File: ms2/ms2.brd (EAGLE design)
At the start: 100 x 100 mm, 127 parts, among them J1 POWERPOLE_POWER25A, J10 RS485_1, J11 I2C, J12 TTL_SERIAL, J13 Radio, J14 RS485_3, J2 RAIN, J3 ADC1, J4 ON, J5 D1, J6 D2, J7 ADC2, J8 LED-EN, J9 RS485_2, Q1 DMG6602SVT, Q2 DMG6602SVT, Q3 DMG6602SVT, Q4 DMG6602SVT, U1 LT1934ES6TRMPBF, U2 LT1934ES6TRMPBF, U3 DS3231SN, U4 ISL3179EIBZ, U5 ISL3179EIBZ, U6 ISL3179EIBZ, X1 KUSBVX-BS1N

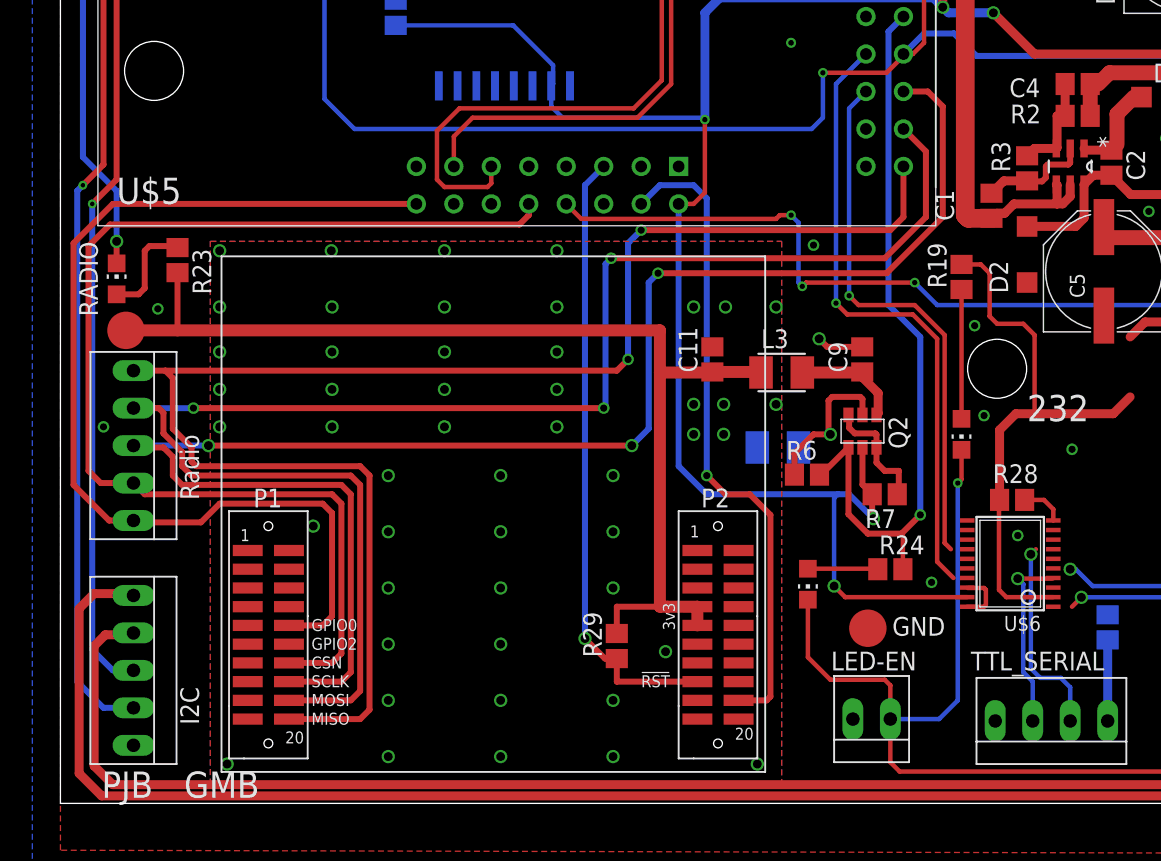
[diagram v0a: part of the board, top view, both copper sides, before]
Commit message: CC1120 rotated
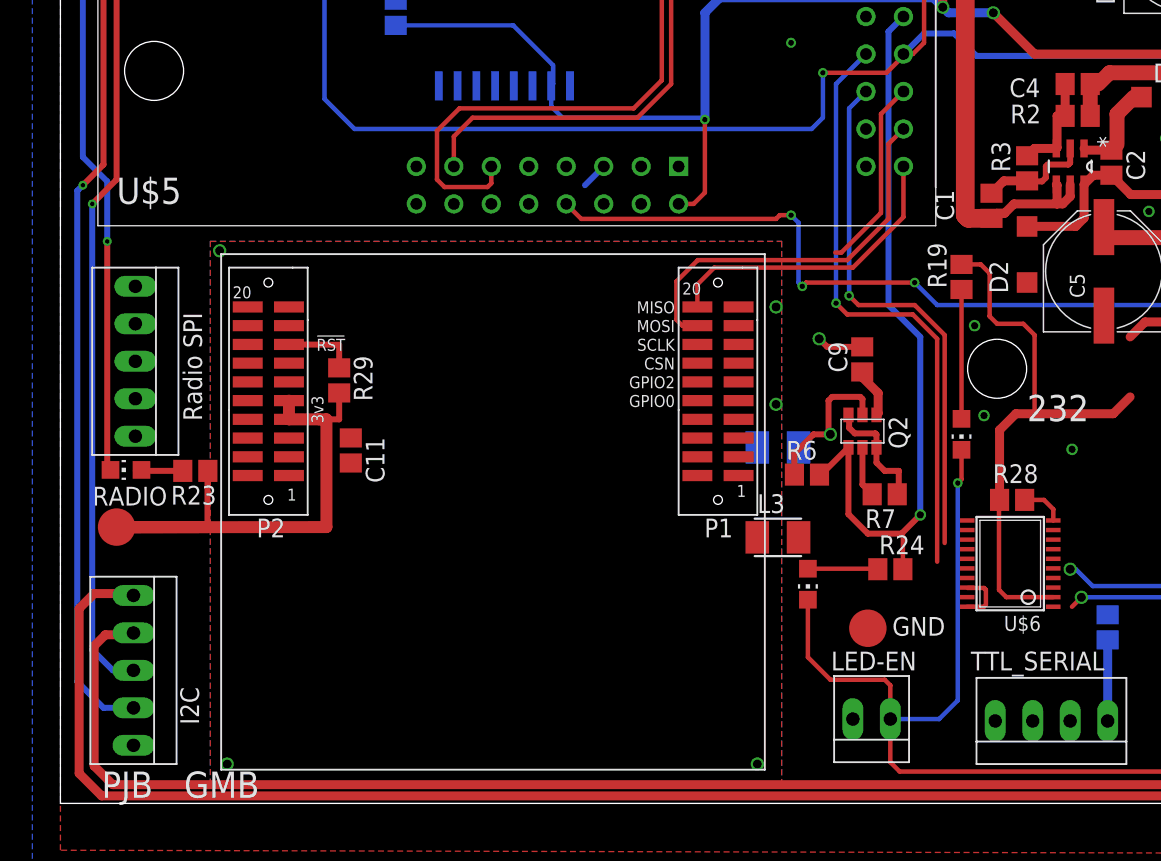
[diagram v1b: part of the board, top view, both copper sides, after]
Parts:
- J13: value Radio -> Radio SPI
- moved R29 26.0 mm to (18.9, 28.7), turned to 270 degrees
- moved C11 25.3 mm to (19.7, 23.9), turned to 270 degrees
- moved U$8 16.5 mm to (29.5, 27.9), turned to 180 degrees
- moved R23 14.3 mm to (9.14, 22.5), turned to 0 degrees
- moved RADIO_VCC 13.4 mm to (3.81, 18.7)
- moved LED8 13.0 mm to (4.45, 22.6), turned to 90 degrees
- moved L3 11.2 mm to (48.6, 18.0)
- moved J13 5.72 mm to (4.95, 28.8)
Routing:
- net SPI_CLK: track 111.0 -> 13.1 mm, vias 3 -> 0
- net SPI_SOMI: track 105.5 -> 20.8 mm, vias 2 -> 0
- net SPI_SIMO: track 109.3 -> 26.8 mm, vias 3 -> 0
- net RADIO_CSN: track 78.8 -> 0.00 mm
- net RADIO_INT: track 70.8 -> 0.00 mm
- net VCC_3V3: track 245.7 -> 195.8 mm, vias 8 -> 6
- net RADIO_CCA_STATUS: track 44.1 -> 0.00 mm, vias 1 -> 0
- net RADIO_!RST: track 42.3 -> 6.76 mm, vias 1 -> 0
- net RADIO_3V3: track 74.8 -> 44.2 mm
- net LGND: track 380.5 -> 394.4 mm
- net TTL_TX: track 13.7 -> 0.00 mm, vias 1 -> 0
- net TTL_RX: track 12.4 -> 0.00 mm, vias 1 -> 0
- net N$24: track 7.47 -> 3.41 mm
- net N$108: track 7.01 -> 3.57 mm
- net UART1_RX: track 45.9 -> 44.3 mm
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
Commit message: Work on MS2
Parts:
- moved J11 118.1 mm to (122.9, 11.2)
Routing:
- net SENSE_3V3: track 327.0 -> 178.7 mm
- net SENSE_5V: track 224.8 -> 99.6 mm
- net SCL: track 113.1 -> 0.00 mm, vias 2 -> 0
- net SDA: track 110.4 -> 0.00 mm, vias 2 -> 0
- net GND: track 29.6 -> 0.00 mm, vias 19 -> 0

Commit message: Added LTSpice schematic of Switch mode + LDO combo.
Work on MS2.
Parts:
- removed JP3: (no value), SparkFun-Passives:SJ_2S
- removed L2, L6: 20uH, rcl:6000-XXXX-RC
- added 12V_OUT: POWERPOLE_POWER25A, powerpoles:POWERPOLE_PAIR_25A
- added 3.4V: TPB2,54, testpad:B2,54
- added C23: 0.1uF, resistor:C0805
- added C24: 100uF, rcl:PANASONIC_E
- added D10, D6, D7, D8, D9: (no value), diode:SMB
- added D11, D12: MBR0530T1G, diode:SOD123
- added F10, F11, F12, F13, F14: MCF0805, farnell-parts:0805
- added JP4: PS EN, pinhead:1X02
- added JP6: 3.3V Out EN, pinhead:1X02
- added Q5: DMG6602SVT, farnell-parts:TSOT26
- added R33, R35: 100K, resistor:R0805
- added R34, R36, R37: 1M, resistor:R0805
- added U7: TPD2E001IDRLRQ1, Texas Instruments_By_element14_Batch_1:SOT50P160X60-5N
- added U8, U9: TPS79333DBVR, CC11x:SOT95P280X145-5N
- C16: value 330uF -> 1uF; device rcl:E5-8,5 -> resistor:C0805
- C17: value (none) -> 0.1uF
- C18: value (none) -> 2.2uF; device resistor:B/3528-21R -> resistor:C0805
- C6: value 330uF -> 2.2uF; device rcl:E5-8,5 -> resistor:C0805
- C7: value (none) -> 100uF; device resistor:C0805 -> rcl:PANASONIC_E
- C8: value (none) -> 1uF; device resistor:B/3528-21R -> resistor:C0805
- JP1: device SparkFun-Passives:SJ_2S-NO -> pinhead:1X05
- JP2: value (none) -> 5V Out EN; device SparkFun-Passives:SJ_2S-NO -> pinhead:1X02
- R3: value 604K -> 562K
- R4: value 100K -> 1M
- moved C18 405.4 mm to (0.00, -315.7), turned to 0 degrees
- moved C17 386.0 mm to (0.00, -310.1), turned to 0 degrees
- moved C16 378.4 mm to (0.00, -294.1)
- moved JP1 206.2 mm to (4.83, -143.1), turned to 0 degrees
- moved JP2 193.4 mm to (1.02, -95.9), turned to 0 degrees
- moved R12 171.4 mm to (-0.10, -120.0)
- moved R4 111.8 mm to (115.0, 47.2)
- moved LED11 63.9 mm to (156.2, 21.7)
- moved Q4 63.9 mm to (150.1, 25.7)
- moved R26 63.9 mm to (156.2, 26.0)
- moved R13 63.9 mm to (151.8, 26.2)
- moved VCC_S 63.9 mm to (144.7, 27.8)
- moved C5 62.5 mm to (131.1, 52.0)
- moved C1 56.3 mm to (119.3, 43.8), turned to 270 degrees
- moved D2 55.9 mm to (121.1, 43.4)
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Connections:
- net ADC_3V3 renamed N$40
- net RADIO_INT renamed RADIO_GPIO0
- net RGND renamed RADIO_GND
- net RS485_N_3 renamed RS4853_N
- net RS485_P_1 renamed RS4851_P
- net RS485_P_2 renamed RS4852_P
- net RS485_P_3 renamed RS4853_P
- net SCL renamed I2C_SCL
- net SDA renamed I2C_SDA
- net SPI_CLK renamed RADIO_SPI_CLK
- net SPI_SIMO renamed RADIO_SPI_MOSI
- net SPI_SOMI renamed RADIO_SPI_MISO
- net TXEN renamed TX_EN
- removed net AGND: AGND.TP, C10.2, J3.3, J7.3, JP5.2, R9.1, U$5.A1, U$5.A11, U$5.A12, U$5.A2
- removed net DC_IN: D1.A, J4.2, Q1.P$2, R5.2
- removed net N$107: C4.1, C5.+, D3.A, L1.2, L2.1, R2.2
- removed net N$14: 5V.TP, C16.+, C17.1, C18.+, JP2.1, L6.2
- removed net RADIO_CCA_STATUS: U$5.C42, U$8.GPIO3
- removed net RS485_N_1: J10.2, R30.1, U4.7
- removed net RS485_N_2: J9.2, R27.1, U5.7
- removed net USB_VCC: U$5.A13, U$5.A3, U$5.B23, X1.1
- removed net VCC_3V3: C19.2, F3.2, JP1.1, Q2.P$2, Q4.P$2, R13.2, R18.2, R7.2, U$5.B22, U$5.C40, U$6.19, U3.2
- removed net VCC_HP2_SW: C12.1, Q3.P$4, U2.4, U2.5
- new net +12V: C3.+, D6.C, F11.2, JP4.1, VCC.TP
- new net +3V3: C19.2, D8.C, F14.2, F3.2, JP6.2, Q2.P$2, Q4.P$2, R13.2, R18.2, R7.2, U$5.B22, U$5.C40, U$6.19, U3.2
- new net +3V4: 3.4V.TP, C4.1, C5.+, C8.1, D3.A, L1.2, R2.2, R36.2, U8.1, U8.3
- new net BLUE: JP1.5
- new net GNDA: AGND.TP, C10.2, D10.A, J3.3, J7.3, JP5.2, R9.1, U$5.A1, U$5.A11, U$5.A12, U$5.A2
- new net GREEN: F14.1, JP1.4
- new net N$29: C12.1, D12.C, U2.5
- new net N$3: C14.1, C15.+, C16.1, D5.A, L5.2, R20.2, R37.2, U9.1, U9.3
- new net N$32: C6.1, C7.+, JP6.1, U8.5, VCC_3V.TP
- new net N$34: U$5.C52
- new net N$35: U$5.C50
- new net N$36: U$5.A8
- new net N$37: U$5.A5
- new net N$38: U$5.A7
- new net N$39: U$5.A15
- new net N$41: U$5.C44
- new net N$42: U$5.C41
- new net N$43: Q5.P$3, Q5.P$6, R12.1
- new net N$44: F10.2, Q5.P$2, R12.2
- new net N$45: C1.1, D11.C, U1.5
- new net N$46: R33.1, U1.4
- new net N$47: D11.A, JP4.2, Q3.P$2, R11.2, R33.2, R4.2
- new net N$48: R35.1, U2.4
- new net N$49: D12.A, Q3.P$4, R34.2, R35.2
- new net N$5: D1.C, F11.1
- new net N$54: C17.1, U9.4
- new net RADIO_GPIO2: U$5.C42, U$8.GPIO2
- new net RED: F12.1, JP1.1
- new net RS4852_N: J10.2, J9.2, R27.1, R30.1, U4.7, U5.7
- new net SENSE_12V: 12V_OUT.RED, D9.C, F12.2, Q5.P$4
- new net USB_5V: U$5.A13, U$5.A3, U$5.B23, U7.1, X1.1
- new net YELLOW: F13.1, JP1.3
- net ADC_7: now also D10.C
- net BATV_EN: no longer JP3.2, Q1.P$1, R4.2
- net GND: now also 12V_OUT.BLACK, C16.2, C18.2, C23.2, C24.-, C6.2, C7.-, C8.2, D6.A, D7.A, D8.A, D9.A, JP1.2, Q5.P$5, R34.1, R36.1, R37.1, U8.2, U9.2; no longer C16.-, C18.-, C6.-, C7.2, C8.-, R12.1
- net N$13: now also 5V.TP, C18.1, C24.+, JP2.2, U9.5; no longer C6.+, C7.1, C8.+, JP1.2, L2.2, VCC_3V.TP
- net N$6: now also C23.1, U8.4; no longer C14.1, C15.+, D5.A, L5.2, L6.1, R20.2
- net SENSE_5V: now also D7.C, F13.2, JP2.1; no longer JP2.2
- net SENSE_EN: now also Q1.P$1, Q5.P$1; no longer JP3.1, R12.2
- net TTL_TX: now also U$6.9
- net USB_D_N: now also U7.3
- net USB_D_P: now also U7.5
- net USB_GND: now also U7.4
- net VCC: now also D1.A, F10.1, J4.2, Q1.P$2, R5.2; no longer C1.1, C3.+, D1.C, Q3.P$2, R11.2, U1.4, U1.5, VCC.TP
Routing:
- net VCC_3V3: track 195.8 -> 0.00 mm, vias 6 -> 0
- net AGND: track 113.0 -> 0.00 mm, vias 1 -> 0
- net GNDA: track 0.00 -> 105.5 mm, vias 0 -> 1
- net SENSE_5V: track 99.6 -> 0.00 mm, vias 4 -> 0
- net SENSE_3V3: track 178.7 -> 85.5 mm, vias 2 -> 1
- net SENSE_EN: track 152.6 -> 83.2 mm, vias 5 -> 4
- net N$6: track 52.2 -> 1.92 mm
- net DC_IN: track 48.7 -> 0.00 mm, vias 1 -> 0
- net +3V4: track 0.00 -> 45.1 mm, vias 0 -> 2
- net N$107: track 40.7 -> 0.00 mm
- net +3V3: track 0.00 -> 39.4 mm, vias 0 -> 1
- net N$14: track 29.7 -> 0.00 mm, vias 2 -> 0
- net USB_VCC: track 24.8 -> 0.00 mm, vias 2 -> 0
- net GND: track 0.00 -> 23.9 mm, vias 0 -> 53
- net N$13: track 23.7 -> 0.00 mm
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- added copper zone on layer 1, net N$31

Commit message: "new" power supply implemented on ms2
Added Eagle files for CC1120 breakout.
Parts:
- removed C3: 2200uF, rcl:E5-13
- removed VCC_3V: TPB2,54, testpad:B2,54
- added 3V3: TPB2,54, testpad:B2,54
- added 5V3: 5V B, testpad:B2,54
- added JP10, JP3, JP7, JP8, JP9: (no value), SparkFun-Passives:SJ_2S-NO
- JP4: value PS EN -> (none); device pinhead:1X02 -> SparkFun-Passives:SJ_2S-NO
- moved C24 410.8 mm to (65.8, 83.1), turned to 270 degrees
- moved C18 398.0 mm to (66.6, 76.7)
- moved C17 392.1 mm to (69.8, 75.7), turned to 90 degrees
- moved U9 381.2 mm to (66.8, 73.4), turned to 90 degrees
- moved C16 371.8 mm to (69.6, 71.1), turned to 90 degrees
- moved R35 370.4 mm to (89.3, 76.6)
- moved R34 365.9 mm to (92.8, 76.6)
- moved R37 362.1 mm to (65.9, 67.6), turned to 90 degrees
- moved D12 362.1 mm to (91.7, 78.6)
- moved D6 244.1 mm to (92.9, 88.7)
- moved F11 237.4 mm to (87.7, 89.4), turned to 270 degrees
- moved F10 203.6 mm to (98.9, 52.2), turned to 270 degrees
- moved R12 193.5 mm to (95.3, 48.4), turned to 90 degrees
- moved D10 190.9 mm to (-62.0, -12.9)
- moved D7 190.9 mm to (-62.0, 14.5)
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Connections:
- removed net N$47: D11.A, JP4.2, Q3.P$2, R11.2, R33.2, R4.2
- new net 5V3: 5V3.TP, C14.1, C15.+, C16.1, D5.A, JP8.1, L5.2, R20.2, R37.2, U9.1, U9.3
- new net N$14: U3.3
- new net N$52: U3.4
- net +12V: now also D11.A, F10.1, JP10.1, JP10.2, JP4.2, Q3.P$2, R11.2, R33.2, R4.2; no longer C3.+
- net +3V3: now also JP3.2
- net +3V4: now also JP9.1
- net GND: no longer C3.-
- net N$13: now also JP7.1, JP8.2
- net N$3: now also U3.1; no longer C14.1, C15.+, C16.1, D5.A, L5.2, R20.2, R37.2, U9.1, U9.3
- net N$32: now also 3V3.TP, JP3.1, JP9.2; no longer VCC_3V.TP
- net SENSE_5V: now also JP7.2
- net VCC: no longer F10.1
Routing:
- net LGND: track 391.0 -> 13.3 mm, vias 8 -> 0
- net DIO_1: track 119.0 -> 0.00 mm, vias 1 -> 0
- net RAIN: track 117.7 -> 0.00 mm, vias 1 -> 0
- net GNDA: track 105.5 -> 0.00 mm, vias 1 -> 0
- net VCC: track 101.6 -> 6.01 mm, vias 1 -> 0
- net DIO_2: track 93.1 -> 0.00 mm, vias 1 -> 0
- net SENSE_12V: track 0.00 -> 87.5 mm
- net +3V3: track 39.4 -> 122.5 mm
- net SENSE_3V3: track 85.5 -> 10.00 mm, vias 1 -> 0
- net RADIO_GPIO0: track 0.00 -> 70.1 mm, vias 0 -> 1
- net ADC_1: track 64.5 -> 0.00 mm, vias 1 -> 0
- net RADIO_CSN: track 0.00 -> 61.5 mm, vias 0 -> 1
- net SENSE_5V: track 0.00 -> 60.9 mm, vias 0 -> 1
- net ADC_2: track 59.9 -> 0.00 mm, vias 1 -> 0
- net RADIO_SPI_CLK: track 13.1 -> 67.1 mm, vias 0 -> 1
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- added copper zone on layer 1, net N$33
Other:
- board text added: "MS2"
- board text removed: "MS1"

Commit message: More MS2 layout work.
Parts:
- removed D10: (no value), diode:SMB
- removed JP1: (no value), pinhead:1X05
- removed U$6: TXS0108E, basestation:TSSOP20
- added H1: JST-S06B-PASK-2, CC11x:JST-PA-6-SE
- added R38: 1M, resistor:R0805
- added U10: TXS0108E, basestation:TSSOP20
- F12: value MCF0805 -> 250mA
- JP5: value GND-LINK -> LINK
- LED10: value BAT_EN -> RADIO_EN
- X1: value KUSBVX-BS1N -> 67068-9000; device con-kycon:KUSBVX-BS1N -> con-usb-3:USB-B-H
- moved 12V_OUT 154.5 mm to (94.9, 34.3), turned to 270 degrees
- moved LED11 154.2 mm to (32.5, 113.9)
- moved R26 154.0 mm to (32.5, 117.8)
- moved F14 141.0 mm to (60.0, 88.6), turned to 180 degrees
- moved Q4 140.4 mm to (61.5, 37.3), turned to 90 degrees
- moved F13 137.7 mm to (60.0, 86.7), turned to 180 degrees
- moved R17 137.1 mm to (49.7, 88.8), turned to 0 degrees
- moved F12 134.6 mm to (60.0, 84.9), turned to 180 degrees
- moved LED4 133.9 mm to (45.9, 88.8), turned to 90 degrees
- moved R22 133.0 mm to (49.7, 86.7), turned to 0 degrees
- moved LED7 129.9 mm to (45.9, 86.7), turned to 90 degrees
- moved R18 128.8 mm to (49.7, 84.7), turned to 0 degrees
- moved F9 127.8 mm to (97.8, 8.89), turned to 90 degrees
- moved LED5 125.9 mm to (45.9, 84.7), turned to 90 degrees
- moved F1 119.4 mm to (32.6, 95.2), turned to 90 degrees
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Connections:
- removed net 485_3V3: C20.1, C21.1, C22.1, U4.8, U5.8, U6.8
- removed net BATV_EN: R25.2
- removed net BLUE: JP1.5
- removed net GREEN: F14.1, JP1.4
- removed net N$50: LED10.A, R25.1
- removed net RED: F12.1, JP1.1
- removed net YELLOW: F13.1, JP1.3
- new net ALT_3V3: F12.1, H1.2
- new net ALT_5V: F13.1, H1.3
- new net ALT_9V: F14.1, H1.4
- new net RS4851_N: J10.2, R30.1, U4.7
- net +3V3: now also F12.2, U10.19; no longer D8.C, F14.2, U$6.19
- net 485_RX_1: now also U10.3; no longer U$6.1
- net 485_RX_2: now also U10.4; no longer U$6.3
- net 485_RX_3: now also U10.5; no longer U$6.4
- net 485_TX_1: now also U10.7; no longer U$6.6
- net 485_TX_2: now also U10.8; no longer U$6.7
- net 485_TX_3: now also U10.9; no longer U$6.8
- net ADC_7: no longer D10.C
- net GND: now also H1.1, H1.5, R38.2, U10.11; no longer D7.A, D8.A, D9.A, JP1.2, U$6.11
- net GNDA: no longer D10.A
- net LGND: no longer LED10.C
- net N$8: now also U10.10; no longer U$6.10
- net RS4852_N: no longer J10.2, R30.1, U4.7
- net SENSE_12V: now also F14.2, R17.2; no longer D9.C, F12.2
- net SENSE_3V3: now also C20.1, C21.1, C22.1, R38.1, U10.2, U4.8, U5.8, U6.8; no longer U$6.2
- net SENSE_5V: no longer D7.C
- net SENSE_EN: now also H1.6
- net TTL_RX: now also U10.1; no longer U$6.5
- net TTL_TX: now also U10.6; no longer U$6.9
- net UART1_RX: now also U10.16, U10.17, U10.18, U10.20; no longer U$6.16, U$6.17, U$6.18, U$6.20
- net UART1_TX: now also U10.12, U10.13, U10.14, U10.15; no longer U$6.12, U$6.13, U$6.14, U$6.15
- net USB_5V: now also X1.VBUS; no longer X1.1
- net USB_D_N: now also X1.D-; no longer X1.2
- net USB_D_P: now also X1.D+; no longer X1.3
- net USB_GND: now also X1.GND; no longer X1.4
- net VCC: no longer R17.2
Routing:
- net SENSE_3V3: track 10.00 -> 179.0 mm, vias 0 -> 6
- net GNDA: track 0.00 -> 118.1 mm, vias 0 -> 5
- net SENSE_5V: track 60.9 -> 173.6 mm, vias 1 -> 9
- net VCC: track 6.01 -> 67.5 mm, vias 0 -> 1
- net +3V3: track 122.5 -> 176.3 mm, vias 1 -> 13
- net SENSE_EN: track 30.1 -> 76.6 mm
- net UART1_RX: track 3.63 -> 45.9 mm, vias 0 -> 1
- net 485_RX_3: track 0.00 -> 40.9 mm, vias 0 -> 2
- net 485_TX_3: track 0.00 -> 40.0 mm, vias 0 -> 2
- net UART1_TX: track 0.00 -> 39.9 mm, vias 0 -> 1
- net ADC_2: track 0.00 -> 34.6 mm
- net DIO_2: track 0.00 -> 34.1 mm, vias 0 -> 1
- net 485_3V3: track 33.5 -> 0.00 mm
- net ADC_1: track 0.00 -> 32.2 mm
- net RADIO_!RST: track 4.97 -> 36.6 mm, vias 0 -> 1
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- added copper zone on layer 1, net GNDA
- added copper zone on layer 16, net GNDA
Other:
- board text added: "ALT PWR"
- board text added: "GND"
